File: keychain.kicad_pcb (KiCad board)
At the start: 2 copper layers, 85.8 x 46 mm, 12 parts, among them SW1 SW_Push, SW2 SW_Push, SW3 SW_Push

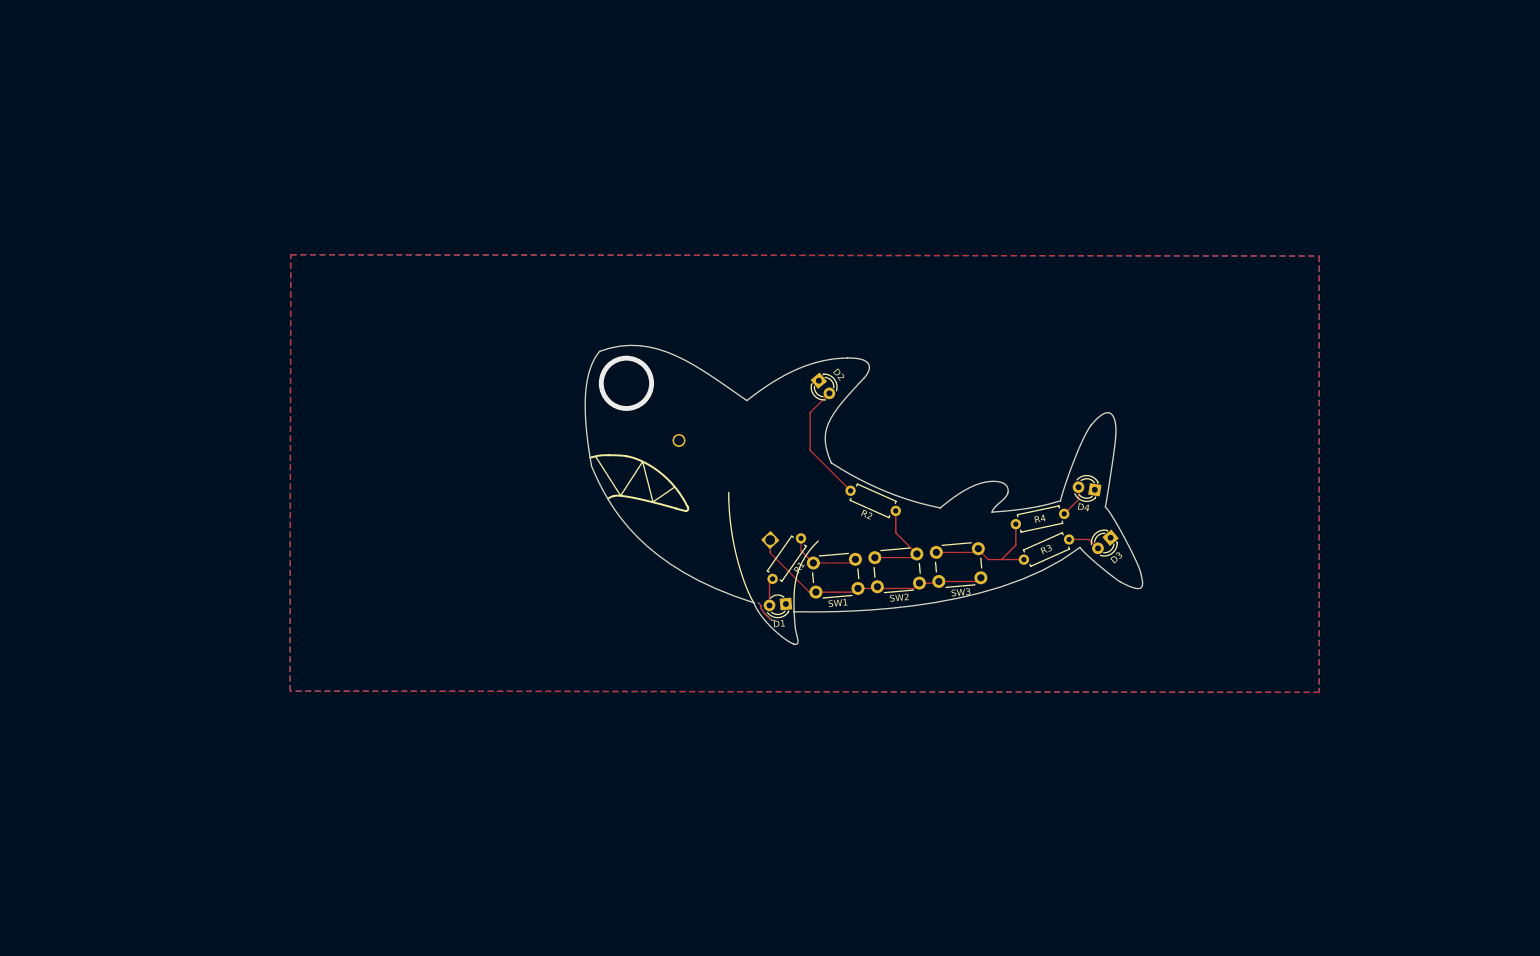
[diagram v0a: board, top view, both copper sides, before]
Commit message: Add 555 transistor circuit
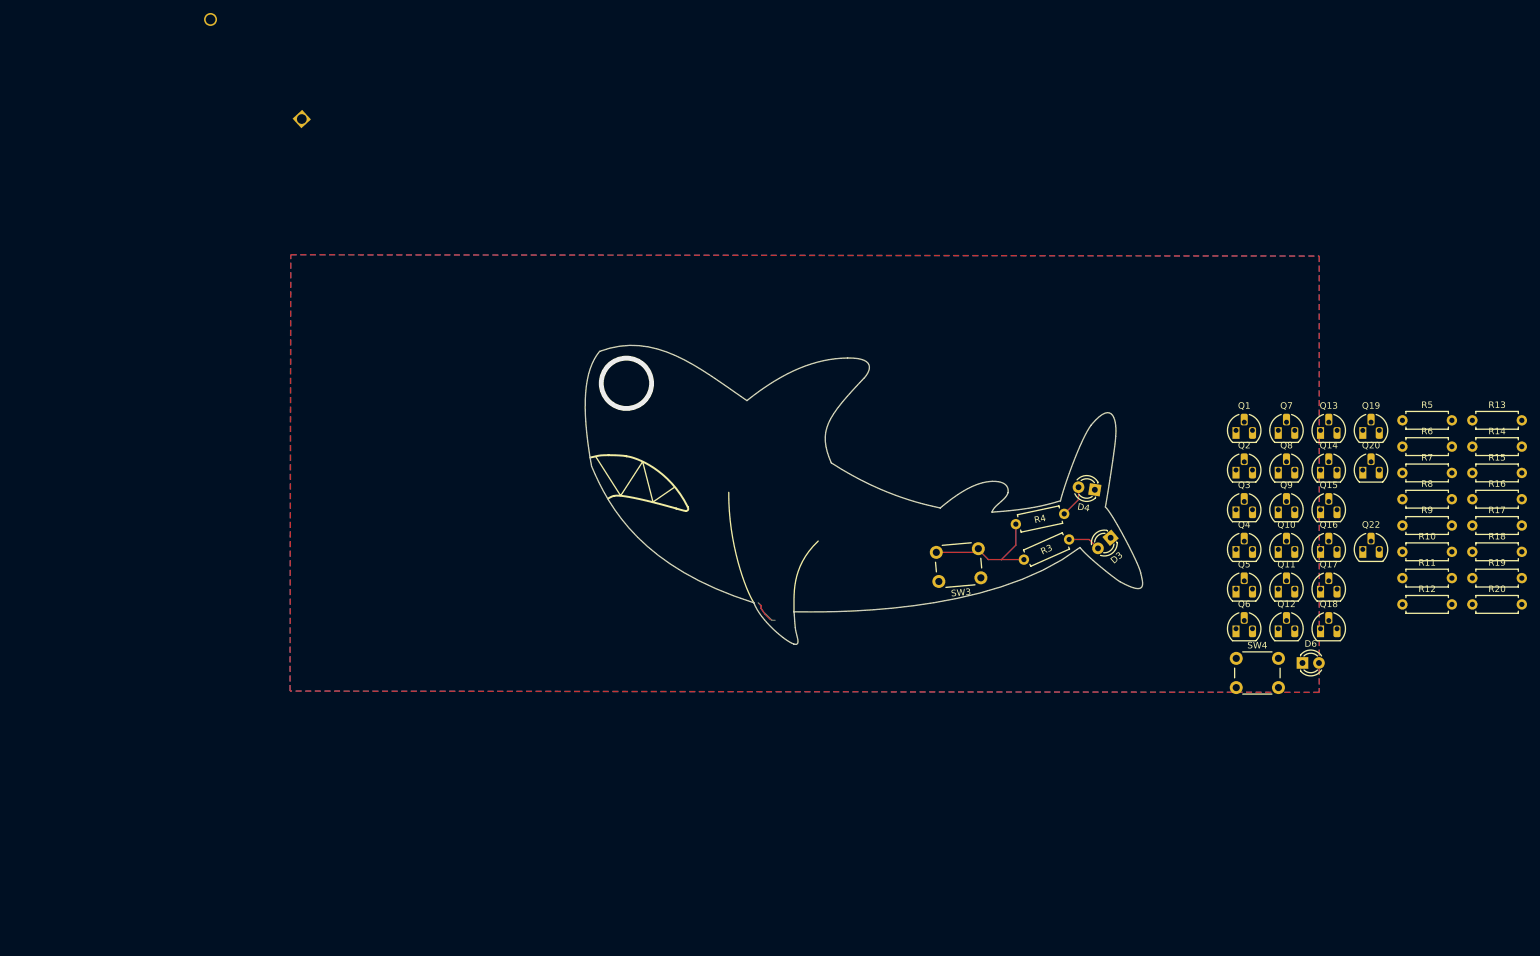
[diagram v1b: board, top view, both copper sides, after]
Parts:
- removed D1, D2: LED, LED_THT:LED_D3.0mm
- removed R1, R2: R, Resistor_THT:R_Axial_DIN0207_L6.3mm_D2.5mm_P7.62mm_Horizontal
- removed SW1, SW2: SW_Push, Button_Switch_THT:SW_PUSH_6mm
- added D6: LED, LED_THT:LED_D3.0mm, F.Cu at (217.5, 126.0)
- added Q1: PNP, Package_TO_SOT_THT:TO-92L_HandSolder, F.Cu at (207.3, 90.2)
- added Q10: PNP, Package_TO_SOT_THT:TO-92L_HandSolder, F.Cu at (213.8, 108.5)
- added Q11: PNP, Package_TO_SOT_THT:TO-92L_HandSolder, F.Cu at (213.8, 114.6)
- added Q12: PNP, Package_TO_SOT_THT:TO-92L_HandSolder, F.Cu at (213.8, 120.7)
- added Q13: PNP, Package_TO_SOT_THT:TO-92L_HandSolder, F.Cu at (220.3, 90.2)
- added Q14: PNP, Package_TO_SOT_THT:TO-92L_HandSolder, F.Cu at (220.3, 96.3)
- added Q15: PNP, Package_TO_SOT_THT:TO-92L_HandSolder, F.Cu at (220.3, 102.4)
- added Q16: NPN, Package_TO_SOT_THT:TO-92L_HandSolder, F.Cu at (220.3, 108.5)
- added Q17: NPN, Package_TO_SOT_THT:TO-92L_HandSolder, F.Cu at (220.3, 114.6)
- added Q18: NPN, Package_TO_SOT_THT:TO-92L_HandSolder, F.Cu at (220.3, 120.7)
- added Q19: NPN, Package_TO_SOT_THT:TO-92L_HandSolder, F.Cu at (226.8, 90.2)
- added Q2: PNP, Package_TO_SOT_THT:TO-92L_HandSolder, F.Cu at (207.3, 96.3)
- added Q20: NPN, Package_TO_SOT_THT:TO-92L_HandSolder, F.Cu at (226.8, 96.3)
- added Q22: NPN, Package_TO_SOT_THT:TO-92L_HandSolder, F.Cu at (226.8, 108.5)
- added Q3: NPN, Package_TO_SOT_THT:TO-92L_HandSolder, F.Cu at (207.3, 102.4)
- added Q4: NPN, Package_TO_SOT_THT:TO-92L_HandSolder, F.Cu at (207.3, 108.5)
- added Q5: NPN, Package_TO_SOT_THT:TO-92L_HandSolder, F.Cu at (207.3, 114.6)
- added Q6: NPN, Package_TO_SOT_THT:TO-92L_HandSolder, F.Cu at (207.3, 120.7)
- added Q7: PNP, Package_TO_SOT_THT:TO-92L_HandSolder, F.Cu at (213.8, 90.2)
- added Q8: PNP, Package_TO_SOT_THT:TO-92L_HandSolder, F.Cu at (213.8, 96.3)
- added Q9: PNP, Package_TO_SOT_THT:TO-92L_HandSolder, F.Cu at (213.8, 102.4)
- added R10: R, Resistor_THT:R_Axial_DIN0207_L6.3mm_D2.5mm_P7.62mm_Horizontal, F.Cu at (232.9, 108.8)
- added R11: R, Resistor_THT:R_Axial_DIN0207_L6.3mm_D2.5mm_P7.62mm_Horizontal, F.Cu at (232.9, 112.9)
- added R12: R, Resistor_THT:R_Axial_DIN0207_L6.3mm_D2.5mm_P7.62mm_Horizontal, F.Cu at (232.9, 117.0)
- added R13: R, Resistor_THT:R_Axial_DIN0207_L6.3mm_D2.5mm_P7.62mm_Horizontal, F.Cu at (243.7, 88.6)
- added R14: R, Resistor_THT:R_Axial_DIN0207_L6.3mm_D2.5mm_P7.62mm_Horizontal, F.Cu at (243.7, 92.7)
- added R15: R, Resistor_THT:R_Axial_DIN0207_L6.3mm_D2.5mm_P7.62mm_Horizontal, F.Cu at (243.7, 96.7)
- added R16: R, Resistor_THT:R_Axial_DIN0207_L6.3mm_D2.5mm_P7.62mm_Horizontal, F.Cu at (243.7, 100.8)
- added R17: R, Resistor_THT:R_Axial_DIN0207_L6.3mm_D2.5mm_P7.62mm_Horizontal, F.Cu at (243.7, 104.8)
- added R18: R, Resistor_THT:R_Axial_DIN0207_L6.3mm_D2.5mm_P7.62mm_Horizontal, F.Cu at (243.7, 108.8)
- added R19: 0ohm, Resistor_THT:R_Axial_DIN0207_L6.3mm_D2.5mm_P7.62mm_Horizontal, F.Cu at (243.7, 112.9)
- added R20: R, Resistor_THT:R_Axial_DIN0207_L6.3mm_D2.5mm_P7.62mm_Horizontal, F.Cu at (243.7, 117.0)
- added R5: R, Resistor_THT:R_Axial_DIN0207_L6.3mm_D2.5mm_P7.62mm_Horizontal, F.Cu at (232.9, 88.6)
- added R6: R, Resistor_THT:R_Axial_DIN0207_L6.3mm_D2.5mm_P7.62mm_Horizontal, F.Cu at (232.9, 92.7)
- added R7: R, Resistor_THT:R_Axial_DIN0207_L6.3mm_D2.5mm_P7.62mm_Horizontal, F.Cu at (232.9, 96.7)
- added R8: R, Resistor_THT:R_Axial_DIN0207_L6.3mm_D2.5mm_P7.62mm_Horizontal, F.Cu at (232.9, 100.8)
- added R9: R, Resistor_THT:R_Axial_DIN0207_L6.3mm_D2.5mm_P7.62mm_Horizontal, F.Cu at (232.9, 104.8)
- added SW4: SW_Push, Button_Switch_THT:SW_PUSH_6mm, F.Cu at (207.3, 125.3)
- moved BT1 97.0 mm to (63.4, 42.2)
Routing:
- net VCC: track 37.9 -> 0.00 mm
- net Net-(D2-A): track 18.8 -> 0.00 mm
- net Net-(R2-Pad1): track 14.7 -> 0.00 mm
- net Net-(R1-Pad1): track 11.3 -> 0.00 mm
- net Net-(D1-A): track 4.29 -> 0.00 mm

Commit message: Placed transistors
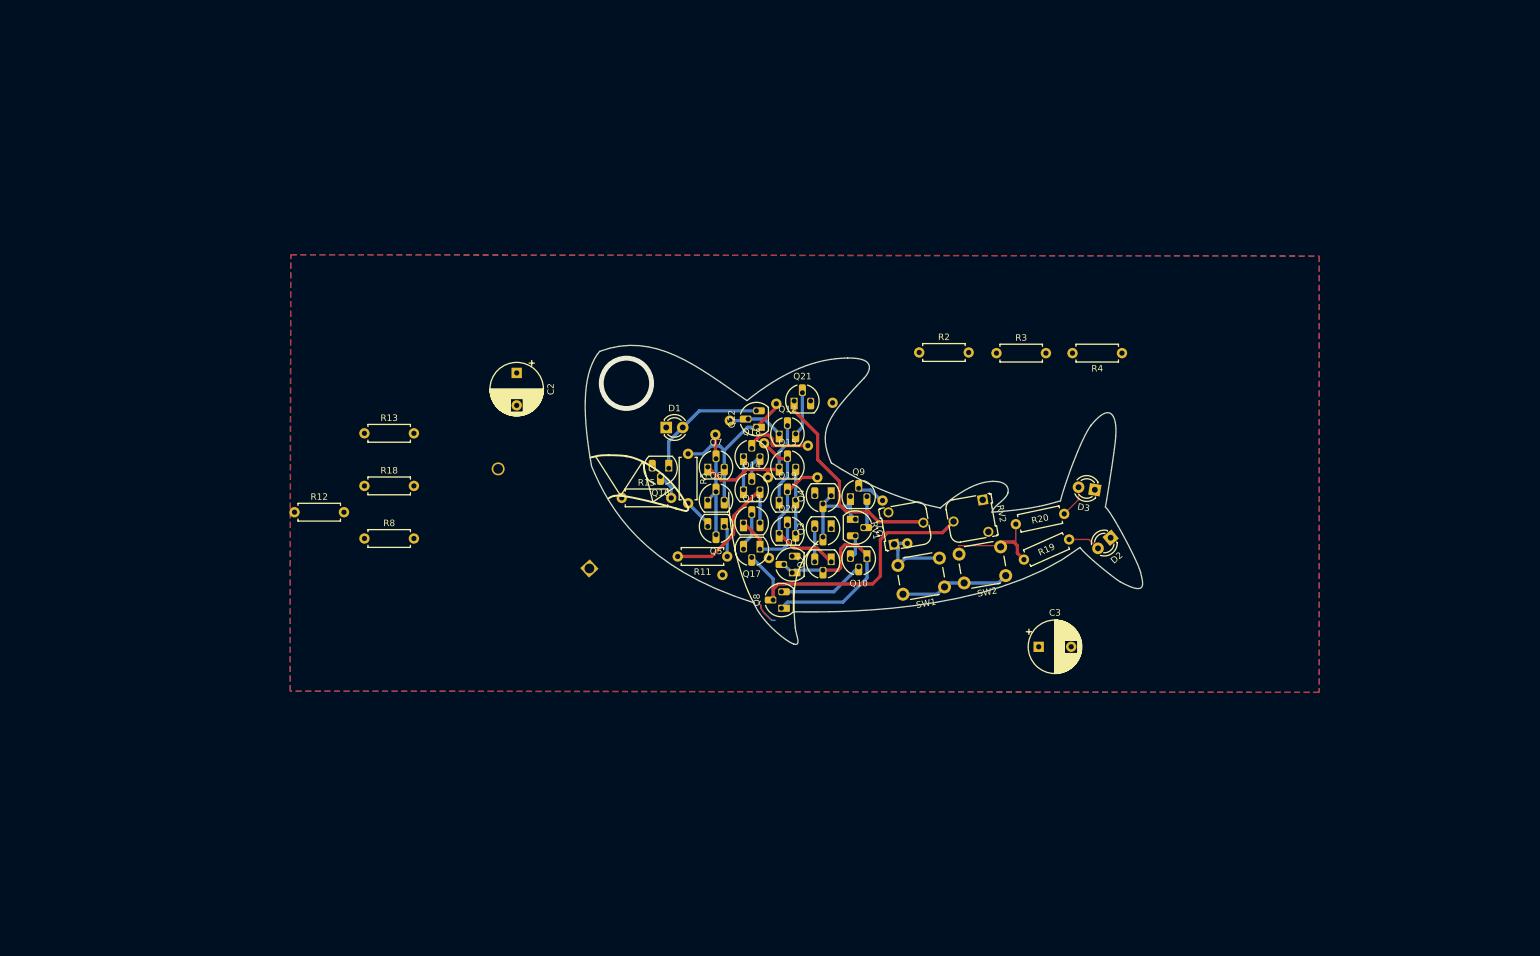
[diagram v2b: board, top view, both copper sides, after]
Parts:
- added C2: C, Capacitor_THT:CP_Radial_D8.0mm_P5.00mm, F.Cu at (96.5, 81.3)
- added C3: 10uF, Capacitor_THT:CP_Radial_D8.0mm_P5.00mm, F.Cu at (176.9, 123.5)
- added Q22: NPN, Package_TO_SOT_THT:TO-92L_HandSolder, F.Cu at (133.4, 89.7)
- added RV1: R_Potentiometer, Potentiometer_THT:Potentiometer_Runtron_RM-065_Vertical, F.Cu at (154.6, 107.7)
- added RV2: R_Potentiometer, Potentiometer_THT:Potentiometer_Runtron_RM-065_Vertical, F.Cu at (168.3, 100.8)
- R10: renamed from R14; moved to B.Cu
- R14: renamed from R13; moved to B.Cu
- R16: renamed from R15; moved to B.Cu
- R17: renamed from R12; moved to B.Cu
- R6: renamed from R10; moved to B.Cu
- R7: renamed from R17; moved to B.Cu
- moved R12 170.9 mm to (62.3, 102.8)
- moved R13 170.9 mm to (73.0, 90.6)
- moved R18 170.9 mm to (73.0, 98.7)
- moved R8 170.9 mm to (73.0, 106.8)
- moved R15 131.6 mm to (112.7, 100.5)
- moved R14 116.6 mm to (127.1, 90.8), turned to -10 degrees
- moved R7 115.5 mm to (129.3, 88.7), turned to 20 degrees
- moved R5 110.2 mm to (122.9, 93.8), turned to -90 degrees
- moved R16 109.1 mm to (135.3, 109.8), turned to -160 degrees
- moved Q16 107.6 mm to (119.9, 96.0), turned to 180 degrees
- moved D1 104.5 mm to (119.5, 89.7)
- moved R11 104.1 mm to (128.9, 109.6), turned to 180 degrees
- moved R10 101.0 mm to (142.8, 97.4), turned to 180 degrees
- moved R17 94.8 mm to (141.3, 92.5), turned to 60 degrees
- moved Q7 94.6 mm to (125.9, 95.8)
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- renumbered D6 to D1, D3 to D2, D4 to D3, Q4 to Q10, Q6 to Q11, Q20 to Q12, Q10 to Q13, Q13 to Q14, Q18 to Q15, Q22 to Q16, Q11 to Q17, Q12 to Q18, Q16 to Q19, Q17 to Q20, Q19 to Q21, Q7 to Q3, Q8 to Q4, Q9 to Q5, Q14 to Q6, Q15 to Q7, Q3 to Q8, Q5 to Q9, R9 to R11, R11 to R12, R16 to R13, R19 to R15, R3 to R19, R5 to R2, R4 to R20, R6 to R3, R7 to R4, R8 to R5, R20 to R8, SW4 to SW1, SW3 to SW2
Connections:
- Q6 pad 3: OUT -> Net-(Q22-C)
- Q7 pad 3: OUT -> Net-(Q22-C)
- R2 pad 1: OUT -> Net-(Q22-C)
- R3 pad 1: OUT -> Net-(Q22-C)
- R4 pad 1: OUT -> Net-(Q22-C)
- R5 pad 1: OUT -> Net-(Q22-C)
- R6 pad 1: OUT -> Net-(Q22-C)
- R7 pad 2: OUT -> Net-(Q22-C)
- R8 pad 1: OUT -> Net-(Q22-C)
- SW1 pad 2: OUT -> Net-(Q22-C)
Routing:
- net THRESHOLD: track 0.00 -> 45.0 mm
- net Net-(Q22-C): track 0.00 -> 38.3 mm
- net Net-(Q1-B): track 0.00 -> 36.1 mm
- net DISCHARGE: track 0.00 -> 32.8 mm
- net Net-(Q13-E): track 0.00 -> 23.7 mm
- net Net-(Q19-B): track 0.00 -> 22.3 mm
- net Net-(Q12-B): track 0.00 -> 20.8 mm
- net OUT: track 0.00 -> 19.6 mm
- net Net-(Q5-B): track 0.00 -> 17.3 mm
- net VCC: track 0.00 -> 17.0 mm
- net GND: track 7.07 -> 22.4 mm
- net Net-(Q11-C): track 0.00 -> 15.1 mm
- net Net-(Q10-B): track 0.00 -> 13.5 mm
- net Net-(Q13-C): track 0.00 -> 12.7 mm
- net Net-(Q15-B): track 0.00 -> 11.5 mm
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
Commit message: Sync
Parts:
- removed C2: C, Capacitor_THT:CP_Radial_D8.0mm_P5.00mm
- removed D2, D3: LED, LED_THT:LED_D3.0mm
- removed R15: 0ohm, Resistor_THT:R_Axial_DIN0207_L6.3mm_D2.5mm_P7.62mm_Horizontal
- removed R19, R20: R, Resistor_THT:R_Axial_DIN0207_L6.3mm_D2.5mm_P7.62mm_Horizontal
- removed SW2: SW_Push, Button_Switch_THT:SW_PUSH_6mm
- added J1: Conn_01x05_Pin, Connector_PinHeader_2.54mm:PinHeader_1x05_P2.54mm_Vertical, B.Cu at (21.6, 130.8)
- added JP1: SolderJumper_2_Bridged, Jumper:SolderJumper-2_P1.3mm_Bridged2Bar_RoundedPad1.0x1.5mm, B.Cu at (25.6, 146.4)
- BT1: footprint Battery:BatteryHolder_MYOUNG_BS-07-A1BJ001_CR2032 -> Battery:BatteryHolder_Multicomp_BC-2001_1x2032; moved to F.Cu
- R10, R14, R16, R17, R6, R7: moved to F.Cu
- moved C3 153.4 mm to (25.6, 149.1), turned to 180 degrees
- moved R4 144.5 mm to (53.2, 125.5), turned to -90 degrees
- moved RV2 142.3 mm to (30.6, 136.8), turned to -90 degrees
- moved R3 135.4 mm to (43.5, 125.5), turned to -90 degrees
- moved R2 131.7 mm to (35.6, 125.5), turned to -90 degrees
- moved RV1 125.0 mm to (30.6, 123.5), turned to -90 degrees
- moved SW1 119.7 mm to (52.3, 161.2), turned to 0 degrees
- moved Q10 114.3 mm to (41.9, 145.6), turned to -90 degrees
- moved Q11 109.9 mm to (47.0, 145.6)
- moved Q2 108.7 mm to (40.3, 139.8), turned to 90 degrees
- moved Q1 107.4 mm to (35.2, 139.8)
- moved Q9 105.5 mm to (52.1, 144.4), turned to -90 degrees
- moved Q8 104.0 mm to (36.8, 144.3), turned to -90 degrees
- moved Q3 103.2 mm to (47.7, 139.8), turned to 90 degrees
- moved Q4 100.3 mm to (52.8, 139.8), turned to 90 degrees
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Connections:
- C3 pad 1: THRESHOLD -> TRIGGER
- Q16 pad 2: Net-(Q16-B) -> Net-(Q12-E)
- Q17 pad 2: THRESHOLD -> TRIGGER
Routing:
- net GND: track 22.4 -> 213.3 mm, vias 0 -> 1
- net Net-(J1-Pin_2): track 38.3 -> 188.2 mm
- net DISCHARGE: track 32.8 -> 105.9 mm
- net Net-(Q19-B): track 22.3 -> 69.5 mm
- net TRIGGER: track 0.00 -> 45.1 mm
- net Net-(Q5-B): track 17.3 -> 53.7 mm
- net Net-(Q9-B): track 4.45 -> 30.8 mm
- net Net-(Q12-B): track 20.8 -> 46.4 mm
- net VCC: track 17.0 -> 42.6 mm
- net THRESHOLD: track 45.0 -> 23.0 mm
- net Net-(Q13-C): track 12.7 -> 32.8 mm
- net Net-(Q1-B): track 36.1 -> 19.4 mm
- net Net-(Q12-C): track 8.66 -> 24.9 mm
- net Net-(R19-Pad1): track 14.5 -> 0.00 mm
- net Net-(Q13-E): track 23.7 -> 10.2 mm
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- removed copper zone on B.Cu, net GND
- removed copper zone on F.Cu, net GND
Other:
- board size 85.8 x 46 mm -> 92.3 x 46.7 mm
- board text added: "1/3"
- board text added: "2/3"
- board text added: "Discharge"
- board text added: "GND"
- board text added: "Open 555"
- board text added: "Output"
- board text added: "SR Latch"
- board text added: "Threshold"
- board text added: "Threshold OPAmp"
- board text added: "Trigger"
- board text added: "Trigger OPAmp"
- board text added: "VCC"
- board text added: "Voltage devider"
